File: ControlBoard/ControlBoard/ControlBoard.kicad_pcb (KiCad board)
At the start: 2 copper layers, 95 x 50 mm, 17 parts, among them J1 Barrel_Jack_MountingPin, J2 HEADER_10, J3 Arduino_Nano_Header, J4 HEADER_10, J5 HEADER_5, SW1 SW_SPDT, U1 ESP-01v090

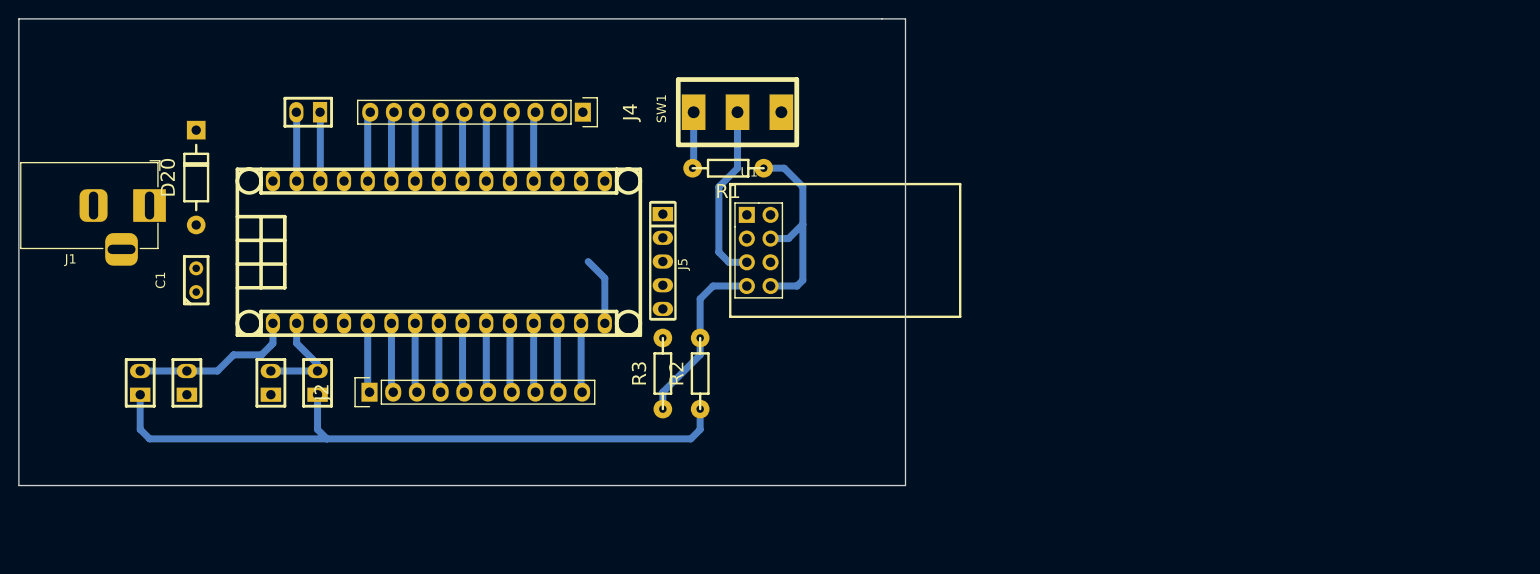
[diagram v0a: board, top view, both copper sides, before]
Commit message: Concluyo diseño de ControlBoard
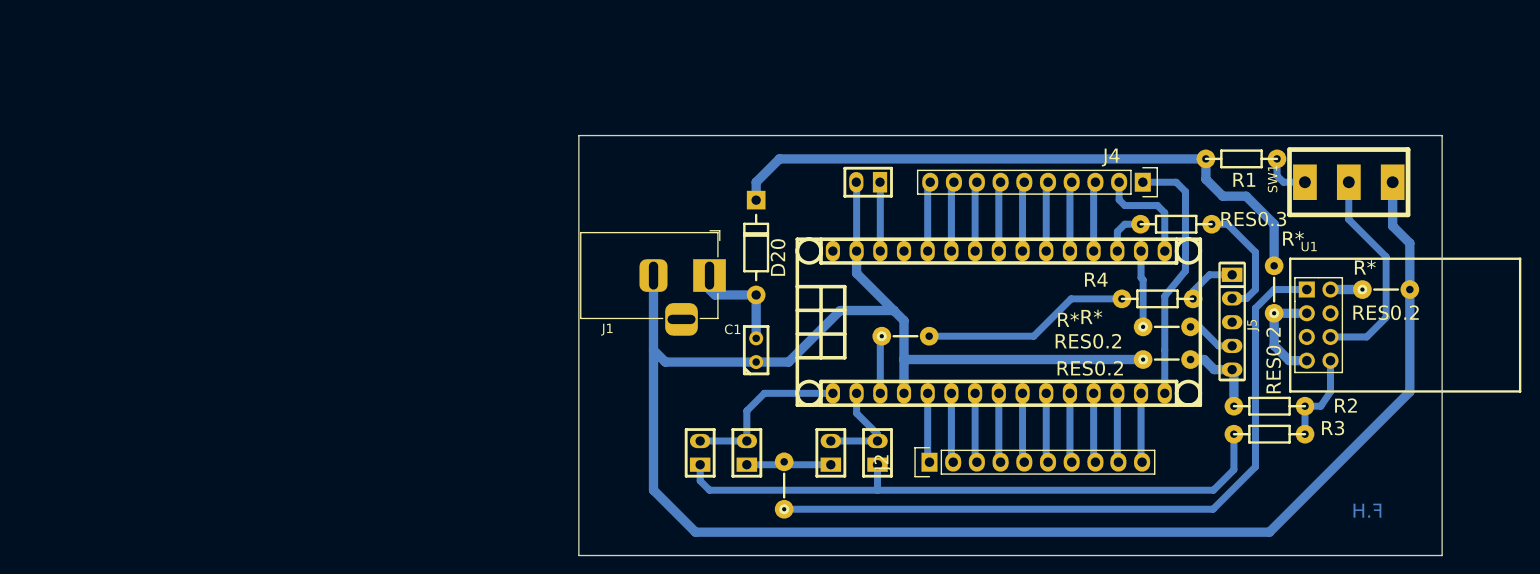
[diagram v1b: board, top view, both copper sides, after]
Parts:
- added R4: 0, EESTN5:RES0.3, F.Cu at (167.0, 85.0)
- added RES0.2: R*, EESTN5:RES0.2, F.Cu at (179.5, 84.0)
- added RES0.2: R*, EESTN5:RES0.2, F.Cu at (191.5, 84.0)
- added RES0.2: R*, EESTN5:RES0.2, F.Cu at (168.0, 91.5)
- added RES0.2: R*, EESTN5:RES0.2, F.Cu at (127.0, 105.0)
- added RES0.2: R*, EESTN5:RES0.2, F.Cu at (168.0, 88.0)
- added RES0.2: R*, EESTN5:RES0.2, F.Cu at (140.0, 89.0)
- added RES0.3: 0, EESTN5:RES0.3, F.Cu at (169.0, 77.0)
- moved SW1 65.9 mm to (187.5, 72.5)
- moved R3 65.1 mm to (179.0, 96.5), turned to 180 degrees
- moved J5 61.3 mm to (175.0, 87.5)
- moved R2 61.3 mm to (179.0, 99.5), turned to 0 degrees
- moved U1 60.5 mm to (183.0, 84.0)
- moved C1 60.5 mm to (124.0, 90.5)
- moved D20 60.5 mm to (124.0, 79.5)
- moved J1 60.5 mm to (119.0, 82.5)
- moved J2 60.5 mm to (154.0, 102.5)
- moved J3 60.5 mm to (150.0, 87.5)
- moved J4 60.5 mm to (154.0, 72.5)
- moved JP1 60.5 mm to (118.0, 101.5)
- moved JP2 60.5 mm to (123.0, 101.5)
- moved JP3 60.5 mm to (137.0, 101.5)
- moved JP4 60.5 mm to (132.0, 101.5)
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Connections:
- J3 pad 27: /5V -> Net-(J3-Pad27)
- J5 pad 3: /5V -> Net-(J5-Pad3)
- U1 pad 1: GND -> /TX
- U1 pad 2: /TX -> GND
- U1 pad 3: Net-(U1-Pad3) -> +3V3
- U1 pad 4: +3V3 -> Net-(U1-Pad4)
- U1 pad 5: /GPIO0 -> Net-(U1-Pad5)
- U1 pad 6: Net-(U1-Pad6) -> /GPIO0
- U1 pad 7: /RX -> +3V3
- U1 pad 8: +3V3 -> /RX
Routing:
- net GND: track 7.39 -> 226.9 mm
- net /TX: track 0.00 -> 84.7 mm
- net +3V3: track 22.8 -> 78.2 mm
- net /RESET: track 0.00 -> 34.2 mm
- net /D12: track 7.36 -> 27.4 mm
- net /AREF: track 0.00 -> 17.7 mm
- net /3V3: track 0.00 -> 13.5 mm
- net /D13: track 0.00 -> 11.5 mm
- net Net-(C1-Pad2): track 0.00 -> 11.4 mm
- net /RX: track 19.0 -> 9.89 mm
- net /RX-A: track 71.9 -> 66.8 mm
- net /GPIO0: track 19.3 -> 23.0 mm
- net Net-(R1-Pad2): track 6.05 -> 5.09 mm
- net Net-(J3-Pad1): track 17.6 -> 18.2 mm
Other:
- board size 95 x 50 mm -> 92.5 x 45 mm
- net class GND added: clearance 0.4, trace_width 1, via_dia 0.5, via_drill 0.4
- net class VCC added: clearance 0.4, trace_width 1, via_dia 0.5, via_drill 0.4
- board text added: "F.H"
